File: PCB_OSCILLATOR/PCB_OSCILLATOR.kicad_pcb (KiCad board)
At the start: 2 copper layers, 99 parts, among them J1 Jumper, J10 Jumper, J11 Jumper, J12 Jumper, J13 Jumper, J14 Jumper, J15 Jumper, J16 Jumper, J2 Jumper, J3 Jumper, J4 Jumper, J5 Jumper, J6 Jumper, J7 Jumper, J8 Jumper, J9 Jumper, P1 POWER SUPPLY, P2 MCLK_EXTERNAL, P3 SPI_AD5270_1, P4 SPI_AD5270_2, P5 SPI_AD9833_1, P6 SPI_AD9833_2, U1 AD5270, U10 ADR291, U2 AD8421, U3 AD9833, U4 AD5270, U5 AD8421, U6 AD9833, U7 ADG819, U8 ADP3303, U9 AD8651

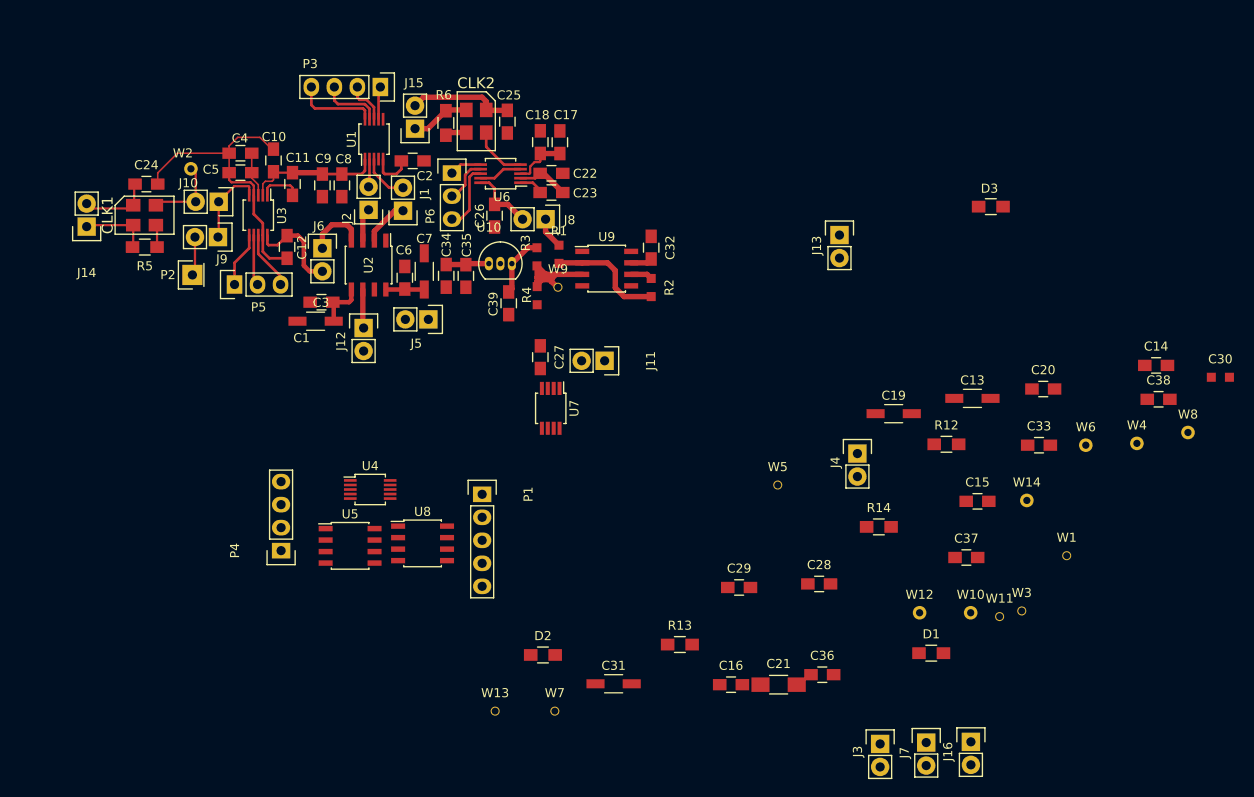
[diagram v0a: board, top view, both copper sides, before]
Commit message: Avance
Falta poner regulador y ultimas etapas.
80% Definir bien puntos para regulador y alimentación.
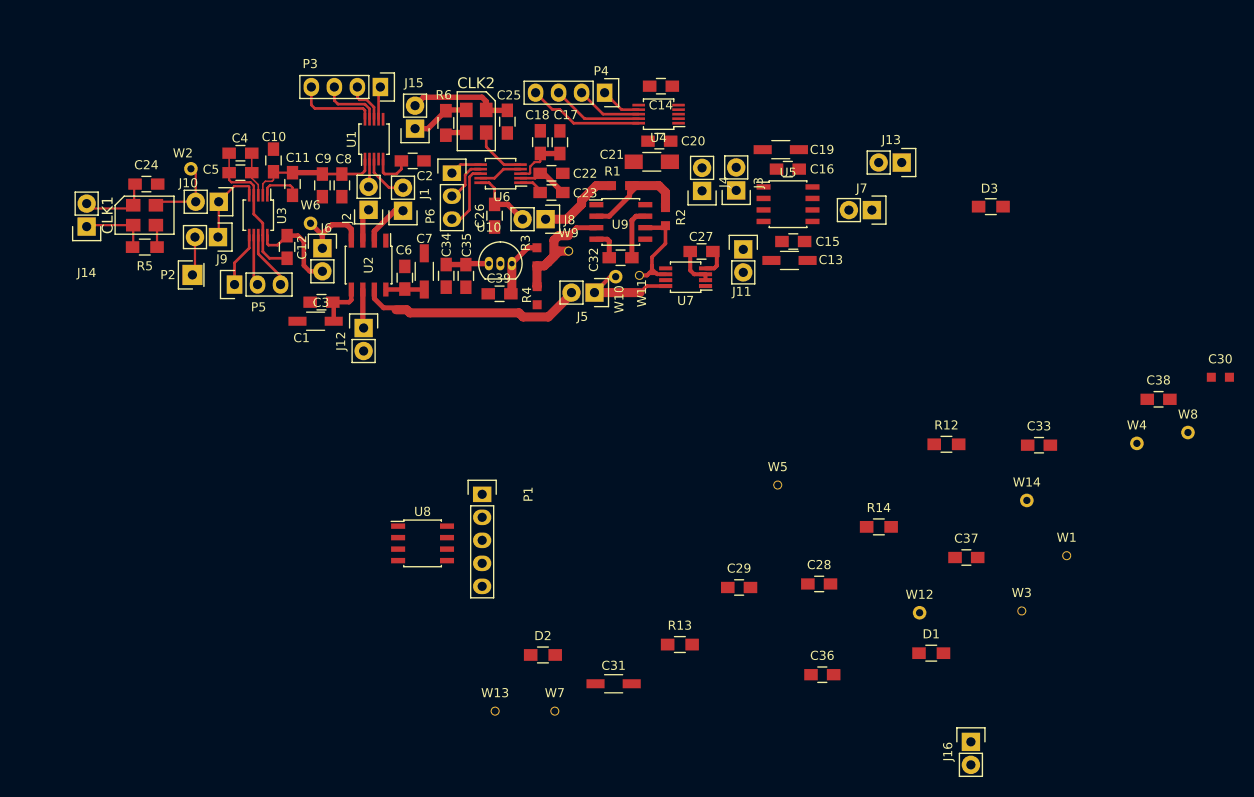
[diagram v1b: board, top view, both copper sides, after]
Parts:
- moved W6 89.0 mm to (91.6, 84.9)
- moved J3 63.1 mm to (138.6, 81.3), turned to 180 degrees
- moved C14 62.8 mm to (130.3, 69.8), turned to 180 degrees
- moved P4 61.9 mm to (124.1, 70.5), turned to 180 degrees
- moved U5 61.3 mm to (144.4, 82.8)
- moved C21 59.4 mm to (129.3, 78.2), turned to 180 degrees
- moved J7 59.1 mm to (153.6, 83.5), turned to 270 degrees
- moved C16 57.3 mm to (144.3, 79.0)
- moved W11 54.8 mm to (128.0, 90.7)
- moved W10 54.0 mm to (125.3, 90.8)
- moved U4 52.3 mm to (130.1, 72.9), turned to 180 degrees
- moved C20 50.5 mm to (130.2, 75.9), turned to 180 degrees
- moved C15 35.2 mm to (144.9, 87.0), turned to 180 degrees
- moved J4 33.7 mm to (134.9, 81.4), turned to 180 degrees
- moved C19 31.7 mm to (143.6, 76.8)
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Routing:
- net Net-(J5-Pad2): track 0.00 -> 26.1 mm
- net /_SYNC_AD5270_2: track 0.00 -> 12.8 mm
- net /BASE_WAVE: track 0.00 -> 11.9 mm
- net /MODULATING_WAVE: track 2.40 -> 12.6 mm
- net /SCLK_AD5270_2: track 0.00 -> 10.0 mm
- net /GND: track 43.6 -> 35.1 mm
- net /DIN_AD5270_2: track 0.00 -> 7.28 mm
- net /VDD: track 48.2 -> 54.7 mm
- net /WAVE_DDS_2: track 3.48 -> 9.46 mm
- net /SDO_AD5270_2: track 0.00 -> 4.53 mm
- net /WAVE_DDS_1: track 6.64 -> 9.94 mm
- net /REF_0.25V: track 16.5 -> 14.7 mm
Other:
- net class Luzbin added: clearance 0.2, trace_width 0.2, via_dia 0.6, via_drill 0.4

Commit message: Pequeños cambios//
//Queda pendiente para mañana
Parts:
- moved W4 76.6 mm to (113.4, 77.0)
- moved W8 72.5 mm to (122.7, 77.7)
- moved C30 72.2 mm to (120.5, 110.8), turned to 270 degrees
- moved J16 65.7 mm to (106.3, 111.8), turned to 180 degrees
- moved C38 52.6 mm to (133.7, 114.8)
- moved W7 52.1 mm to (113.9, 86.9)
- moved W1 48.9 mm to (128.8, 105.7)
- moved W14 45.2 mm to (137.6, 84.7)
- moved W3 44.7 mm to (128.7, 111.0)
- moved W12 41.6 mm to (154.3, 86.6)
- moved C33 38.0 mm to (134.1, 112.3)
- moved D3 37.9 mm to (142.5, 112.2), turned to 180 degrees
- moved D2 36.0 mm to (142.5, 106.9), turned to 180 degrees
- moved C37 30.8 mm to (133.7, 116.9)
- moved W13 30.0 mm to (103.0, 110.2)
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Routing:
- net /REF_2.5V: track 6.87 -> 14.4 mm
- net /WAVE_DDS_2: track 9.46 -> 15.1 mm
- net /MCLK_DDS_2: track 6.17 -> 10.3 mm

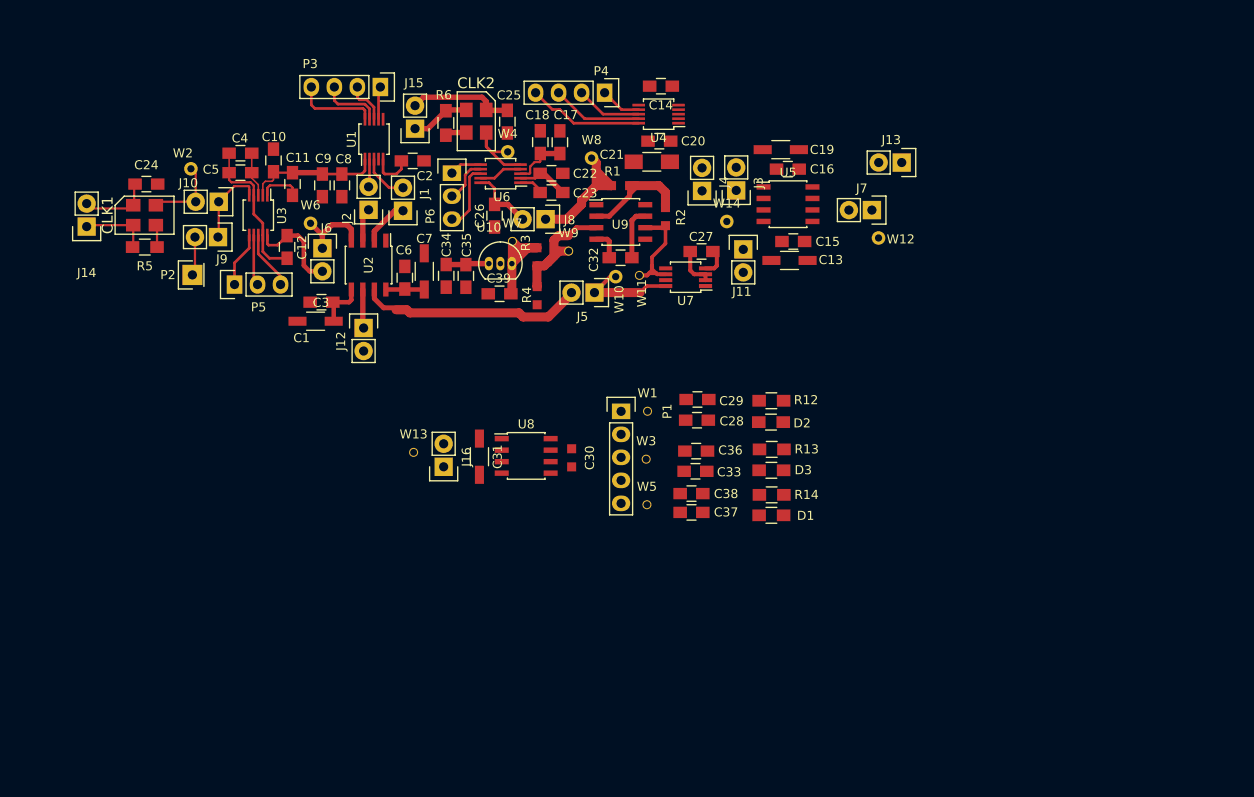
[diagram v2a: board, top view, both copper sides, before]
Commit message: 80% PCB
Terminar conexiones de alimentación, regletas de +12 -12
y tratar de hacer el plano completo para tierra
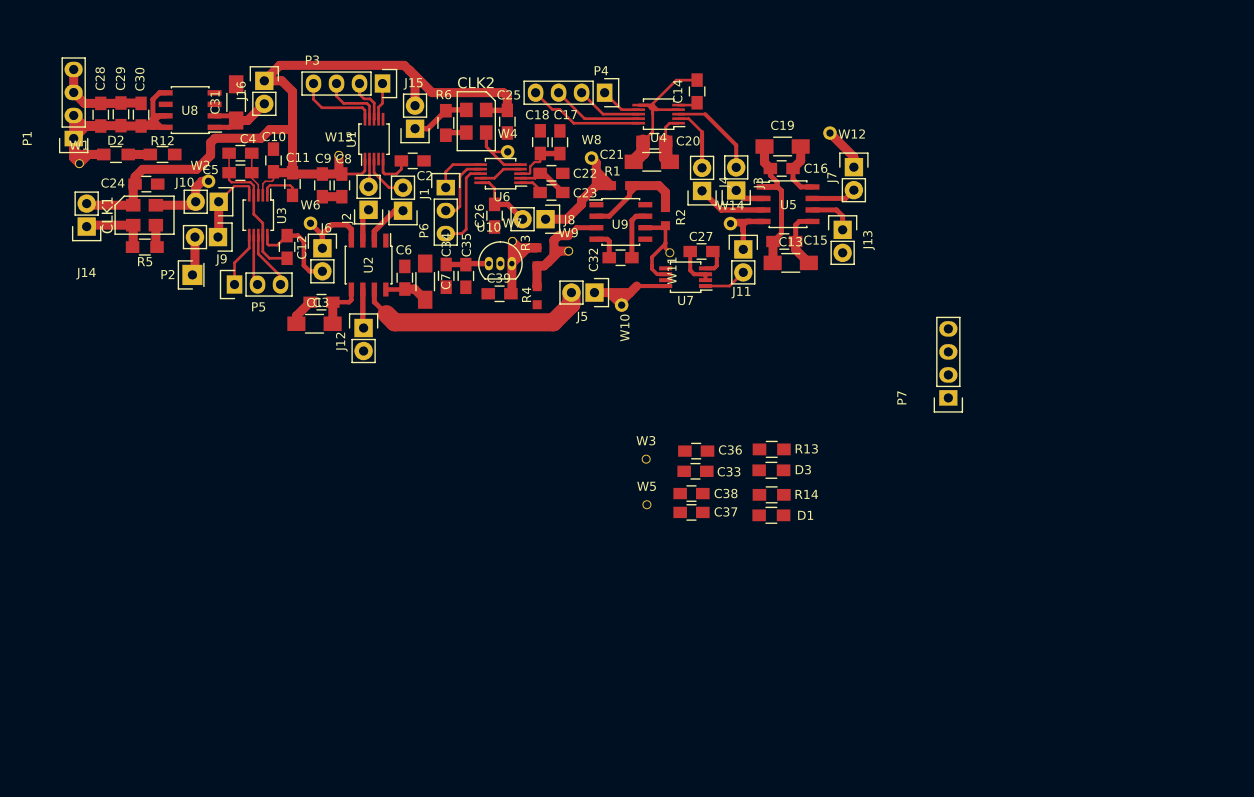
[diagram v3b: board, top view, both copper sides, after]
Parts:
- added P7: CONN_01X04, Socket_Strips:Socket_Strip_Straight_1x04, F.Cu at (162.1, 104.2)
- P1: value POWER SUPPLY -> CONN_01X04; footprint Socket_Strips:Socket_Strip_Straight_1x05 -> Socket_Strips:Socket_Strip_Straight_1x04
- moved D2 78.1 mm to (70.2, 77.3)
- moved C28 74.0 mm to (68.5, 73.0), turned to 90 degrees
- moved R12 72.5 mm to (75.3, 77.3)
- moved C29 71.0 mm to (70.7, 72.9), turned to 90 degrees
- moved W1 68.4 mm to (66.1, 78.3)
- moved P1 67.5 mm to (65.5, 75.6), turned to 90 degrees
- moved C30 60.8 mm to (72.9, 73.0), turned to 90 degrees
- moved U8 53.2 mm to (78.3, 72.4), turned to 180 degrees
- moved C31 47.5 mm to (83.4, 71.6), turned to 90 degrees
- moved J16 47.0 mm to (86.5, 69.2), turned to 0 degrees
- moved W13 33.8 mm to (94.8, 77.4)
- moved W12 12.8 mm to (149.0, 75.0)
- moved J13 9.89 mm to (150.4, 85.7), turned to 0 degrees
- moved J7 5.14 mm to (151.6, 78.7), turned to 0 degrees
- moved W11 4.19 mm to (131.3, 88.2)
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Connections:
- P1 pad 2: /GND -> /+5V
- P1 pad 3: /+12V -> /GND
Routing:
- net /VDD: track 54.7 -> 122.6 mm
- net /GND: track 35.1 -> 89.0 mm
- net /+5V: track 0.00 -> 39.9 mm
- net /A_AD5270_2: track 0.00 -> 11.2 mm
- net /MODULATED_WAVE: track 0.00 -> 9.39 mm
- net Net-(C31-Pad1): track 0.00 -> 9.16 mm
- net Net-(J4-Pad1): track 0.00 -> 7.66 mm
- net /-12V: track 5.44 -> 12.8 mm
- net /+12V: track 4.29 -> 11.5 mm
- net /W_AD5270_2: track 0.00 -> 7.17 mm
- net /BASE_WAVE: track 11.9 -> 17.9 mm
- net Net-(J13-Pad1): track 0.00 -> 5.12 mm
- net Net-(J7-Pad2): track 0.00 -> 4.95 mm
- net /FINAL_WAVE: track 0.00 -> 4.85 mm
- net Net-(J11-Pad2): track 0.00 -> 4.79 mm
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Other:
- net class Default: clearance 0.1778 -> 0.18; trace_width 0.1778 -> 0.2
- net class Luzbin removed
- rule trace_clearance: 0.1778 -> 0.18
- board text added: "plano"

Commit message: PCB 90%
Reacomodar elementos y hacer planos para power integrity y plano de GND
completo por la parte de abajo
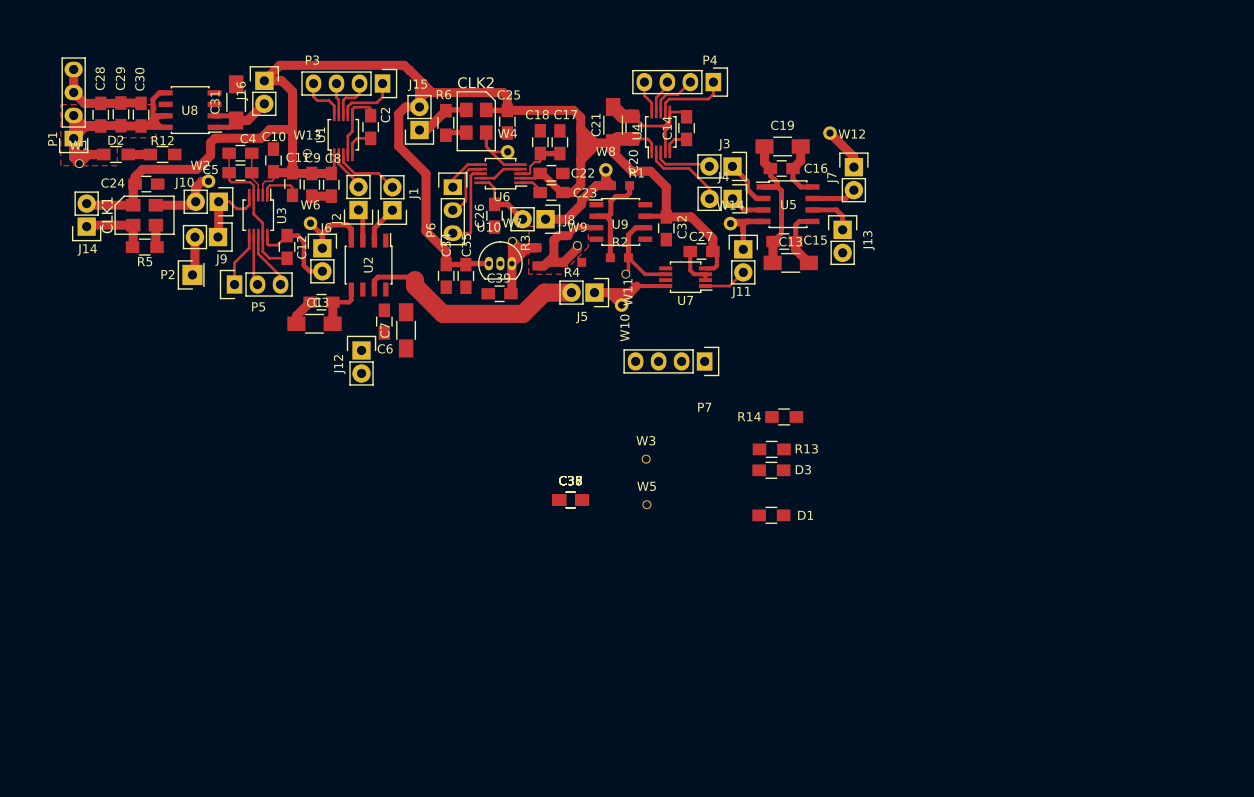
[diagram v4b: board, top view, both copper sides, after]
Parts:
- moved P7 27.2 mm to (135.2, 100.2), turned to 180 degrees
- moved C36 14.9 mm to (120.4, 115.5)
- moved C33 14.1 mm to (120.4, 115.5)
- moved C37 13.4 mm to (120.4, 115.5)
- moved C38 13.4 mm to (120.4, 115.5)
- moved P4 12.1 mm to (136.1, 69.3)
- moved R14 8.71 mm to (143.9, 106.3), turned to 180 degrees
- moved R2 6.82 mm to (125.7, 88.7), turned to 180 degrees
- moved C32 6.01 mm to (130.9, 85.5), turned to 90 degrees
- moved C2 5.96 mm to (98.3, 74.3), turned to 90 degrees
- moved C21 5.89 mm to (125.0, 74.1), turned to 90 degrees
- moved C7 5.78 mm to (102.2, 96.8), turned to 90 degrees
- moved W11 5.40 mm to (126.5, 90.5)
- moved R4 5.38 mm to (120.6, 89.2), turned to 0 degrees
- moved C6 5.34 mm to (99.8, 95.8), turned to 90 degrees
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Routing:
- net /VDD: track 122.6 -> 185.1 mm
- net /_SYNC_AD5270_2: track 12.8 -> 3.64 mm
- net /SCLK_AD5270_2: track 10.0 -> 3.81 mm
- net /+12V: track 11.5 -> 6.47 mm
- net /A_AD5270_2: track 11.2 -> 6.52 mm
- net Net-(J12-Pad1): track 4.41 -> 0.00 mm
- net /_SYNC_AD5270_1: track 8.92 -> 5.14 mm
- net Net-(J4-Pad1): track 7.66 -> 3.93 mm
- net /WAVE_DDS_2: track 15.1 -> 11.5 mm
- net /SDO_AD5270_2: track 4.53 -> 8.04 mm
- net /SCLK_AD5270_1: track 6.95 -> 3.55 mm
- net /SDO_AD5270_1: track 4.12 -> 6.65 mm
- net /W_AD5270_2: track 7.17 -> 9.28 mm
- net Net-(J3-Pad1): track 3.39 -> 5.43 mm
- net /DIN_AD5270_2: track 7.28 -> 5.40 mm
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- added copper zone on F.Cu, net /+5V
- added copper zone on F.Cu, net /REF_0.25V
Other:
- net class Holis added: clearance 0.18, trace_width 0.2, via_dia 0.6, via_drill 0.4
- board text removed: "plano"

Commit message: PCB 95%
Terminar de hacer planos que se crean convenientes//
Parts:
- removed C33, C37: 0.1uF, Capacitors_SMD:C_0805_HandSoldering
- removed C36, C38: 10uF, Capacitors_SMD:C_0805_HandSoldering
- moved D1 60.3 mm to (85.6, 97.5), turned to 90 degrees
- moved R14 54.8 mm to (89.7, 98.8)
- moved W3 45.9 mm to (149.9, 70.3)
- moved D3 38.9 mm to (141.6, 73.3), turned to 0 degrees
- moved R13 38.8 mm to (141.6, 71.1), turned to 180 degrees
- moved W5 18.8 mm to (129.0, 97.2)
- moved P7 8.99 mm to (126.2, 99.1)
- moved R12 6.92 mm to (68.8, 79.7), turned to 0 degrees
- moved J12 3.62 mm to (96.8, 95.4)
- moved W13 1.56 mm to (91.4, 75.7)
- moved C2 0.91 mm to (98.3, 75.2)
- moved C1 0.52 mm to (91.6, 96.0)
- moved C14 0.45 mm to (133.1, 74.9)
- moved C8 0.39 mm to (93.9, 81.1)
- moved C3 0.24 mm to (92.6, 93.6)
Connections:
- P7 pad 1: /+12V -> /-12V
- P7 pad 2: /-12V -> /+12V
- P7 pad 3: /GND -> /-12V
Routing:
- net /+12V: track 6.47 -> 120.7 mm
- net /-12V: track 12.8 -> 88.5 mm
- net /GND: track 88.8 -> 153.5 mm, vias 0 -> 45
- net /VDD: track 185.1 -> 188.6 mm
- net Net-(J12-Pad1): track 0.00 -> 3.39 mm
- net Net-(D1-Pad1): track 0.00 -> 2.74 mm
- net Net-(D3-Pad1): track 0.00 -> 2.22 mm
- net /A_AD5270_2: track 6.52 -> 7.56 mm
- net Net-(C2-Pad1): track 3.51 -> 2.87 mm
- added copper zone on B.Cu, net /GND
- added copper zone on F.Cu, net Net-(C31-Pad1)
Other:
- board outline added: 96.8 x 43.9 mm

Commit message: 98% Completed
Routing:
- added copper zone on F.Cu, net /VDD
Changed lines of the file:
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@@
   )
   (setup
-    (last_trace_width 1)
+    (last_trace_width 0.45)
     (user_trace_width 0.3)
     (user_trace_width 0.35)
@@
     (user_trace_width 2)
     (trace_clearance 0.18)
-    (zone_clearance 0.3)
+    (zone_clearance 0.4)
     (zone_45_only no)
     (trace_min 0.1524)
@@
   (segment (start 85.15 79.95) (end 85.15 79.35) (width 0.1778) (layer F.Cu) (net 3))
   (segment (start 85.15 77.2) (end 85.15 79.35) (width 0.1778) (layer F.Cu) (net 3))
-  (segment (start 91.36 75.67) (end 91.28 75.67) (width 1) (layer F.Cu) (net 4) (status C00000))
-  (segment (start 91.28 75.67) (end 89.65 74.04) (width 1) (layer F.Cu) (net 4) (status 400000))
+  (segment (start 91.36 75.67) (end 91.28 75.67) (width 1) (layer F.Cu) (net 4))
+  (segment (start 91.28 75.67) (end 89.65 74.04) (width 1) (layer F.Cu) (net 4))
   (segment (start 91.78 79.44) (end 93.5 79.44) (width 1) (layer F.Cu) (net 4))
   (segment (start 93.5 79.44) (end 93.89 79.83) (width 1) (layer F.Cu) (net 4))
@@
   (segment (start 87.15 80.75) (end 89.4 80.75) (width 0.25) (layer F.Cu) (net 5))
   (segment (start 86.87232 81.02768) (end 87.15 80.75) (width 0.25) (layer F.Cu) (net 5))
-  (segment (start 92.95 90.24) (end 91.54 90.24) (width 0.5) (layer F.Cu) (net 6))
-  (segment (start 90.25 86.3) (end 89.05 86.3) (width 0.5) (layer F.Cu) (net 6))
-  (segment (start 90.9 86.95) (end 90.25 86.3) (width 0.5) (layer F.Cu) (net 6))
-  (segment (start 90.9 89.6) (end 90.9 86.95) (width 0.5) (layer F.Cu) (net 6))
-  (segment (start 91.54 90.24) (end 90.9 89.6) (width 0.5) (layer F.Cu) (net 6))
+  (segment (start 89.05 86.3) (end 90.28 86.3) (width 1) (layer F.Cu) (net 6))
+  (segment (start 91.81 90.24) (end 92.95 90.24) (width 1) (layer F.Cu) (net 6))
+  (segment (start 90.78 89.21) (end 91.81 90.24) (width 1) (layer F.Cu) (net 6))
+  (segment (start 90.78 86.8) (end 90.78 89.21) (width 1) (layer F.Cu) (net 6))
+  (segment (start 90.28 86.3) (end 90.78 86.8) (width 1) (layer F.Cu) (net 6))
   (segment (start 89.05 86.3) (end 89.2 86.3) (width 0.45) (layer F.Cu) (net 6))
   (segment (start 89.35 86.6) (end 89.05 86.3) (width 0.45) (layer F.Cu) (net 6))
@@
   (segment (start 94.76 78.59) (end 96.94 80.77) (width 0.3) (layer F.Cu) (net 31))
   (segment (start 96.94 80.77) (end 96.94 80.93) (width 0.3) (layer F.Cu) (net 31))
-  (segment (start 92.95 87.7) (end 92.95 86.25) (width 0.55) (layer F.Cu) (net 32))
-  (segment (start 92.95 86.25) (end 91.64 84.94) (width 0.55) (layer F.Cu) (net 32))
+  (segment (start 92.95 87.7) (end 92.95 86.25) (width 1) (layer F.Cu) (net 32))
+  (segment (start 92.95 86.25) (end 91.64 84.94) (width 1) (layer F.Cu) (net 32))
   (segment (start 96.145 86.85) (end 96.145 85.595) (width 0.6) (layer F.Cu) (net 32))
-  (segment (start 92.95 86.15) (end 92.95 87.7) (width 0.6) (layer F.Cu) (net 32))
-  (segment (start 94 85.1) (end 92.95 86.15) (width 0.6) (layer F.Cu) (net 32))
-  (segment (start 95.65 85.1) (end 94 85.1) (width 0.6) (layer F.Cu) (net 32))
   (segment (start 96.145 85.595) (end 95.65 85.1) (width 0.6) (layer F.Cu) (net 32))
+  (segment (start 95.65 85.1) (end 94 85.1) (width 0.6) (layer F.Cu) (net 32))
+  (segment (start 94 85.1) (end 92.95 86.15) (width 0.6) (layer F.Cu) (net 32))
+  (segment (start 92.95 86.15) (end 92.95 87.7) (width 0.6) (layer F.Cu) (net 32))
   (segment (start 130.31 77.05) (end 130.31 78.24) (width 0.3) (layer F.Cu) (net 33))
   (segment (start 131.3 79.23) (end 135.11 79.23) (width 0.3) (layer F.Cu) (net 33))
@@
       )
     )
+  )
+  (zone (net 4) (net_name /VDD) (layer F.Cu) (hatch edge 0.508)
+    (connect_pads (clearance 0.4))
+    (min_thickness 0.2)
+    (fill yes (arc_segments 16) (thermal_gap 0.508) (thermal_bridge_width 0.508) (smoothing fillet))
+    (polygon
+      (pts
+        (xy 125.79 66.19) (xy 125.84 70.8) (xy 129.56 70.86) (xy 129.64 75.29) (xy 129.68 78.74)
+        (xy 137.46 85.83) (xy 137.44 90.89) (xy 123.16 90.75) (xy 123.09 84.65) (xy 122.57 84.65)
+        (xy 115.09 84.88) (xy 115 91.36) (xy 101.64 91.14) (xy 101.42 80.73) (xy 76.5 80.01)
+        (xy 76.39 84.32) (xy 64.15 84.19) (xy 64.19 80.96) (xy 64.19 79.13) (xy 70.99 78.97)
+        (xy 70.97 75.92) (xy 75.1 75.9) (xy 75.11 75.84) (xy 75.11 75.71) (xy 75.1 75.41)
+        (xy 86.18 75.44) (xy 86.35 75.23) (xy 88.38 73.21) (xy 88.38 72.83) (xy 88.33 70.02)
+        (xy 84.73 70.08) (xy 84.69 66.18) (xy 125.79 66.19)
+      )
+    )
